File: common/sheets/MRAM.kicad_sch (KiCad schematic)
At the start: 2 parts, among them U11 MR25H10

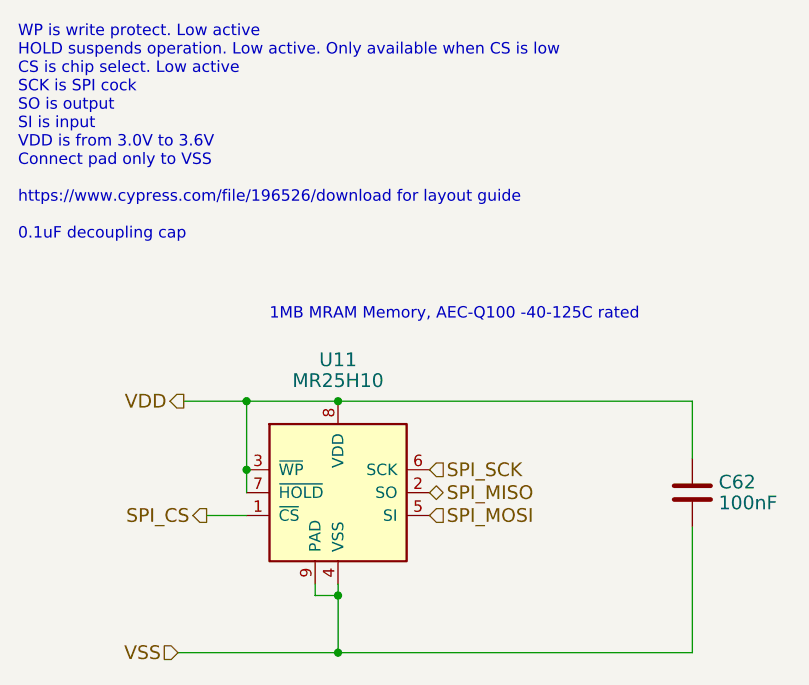
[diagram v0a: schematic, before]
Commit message: move commonly used hierarchical sheets to common/sheets for easy reuse
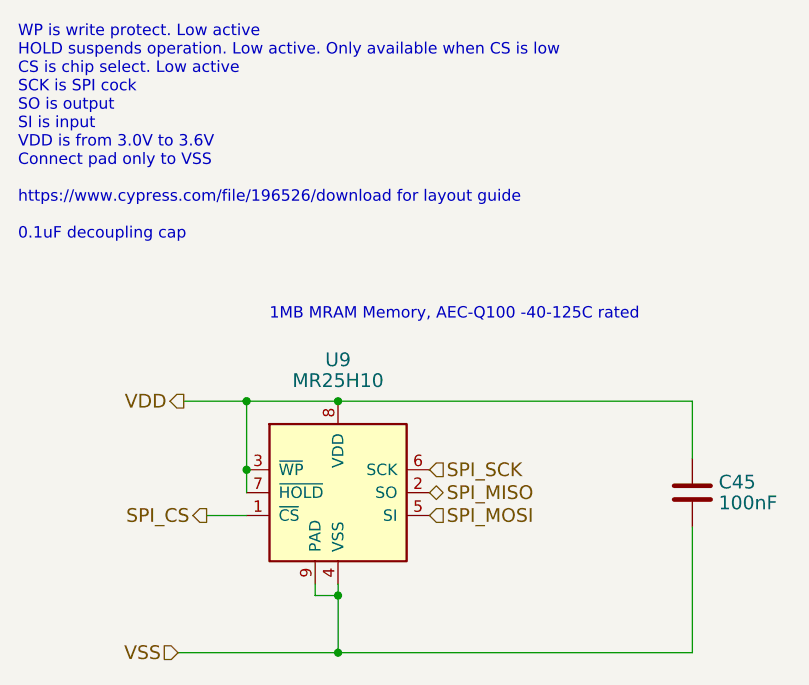
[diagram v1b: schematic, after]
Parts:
- renumbered C62 to C45, U11 to U9
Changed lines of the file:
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@@
 		(on_board yes)
 		(dnp no)
-		(property "Reference" "C62"
+		(property "Reference" "C45"
 			(at 201.041 118.2116 0)
 			(effects
@@
 				)
 			)
-			(project ""
+			(project "comm_board"
 				(path "/a863a5ec-a5d4-4f54-be53-e8c01d5e3ac4/53f12969-e593-459a-9671-cc23a5a9aea0/96ad4f73-2856-49c5-b898-35474412a80c"
 					(reference "C47")
@@
 				)
 			)
-			(project ""
+			(project "AVIONICS_BOARD"
 				(path "/f6cc00ab-17f1-4973-862f-7ac95fe70668/00000000-0000-0000-0000-00005ea31c93/00000000-0000-0000-0000-00006310c53d"
 					(reference "C45")
@@
 		(on_board yes)
 		(dnp no)
-		(property "Reference" "U11"
+		(property "Reference" "U9"
 			(at 158.75 104.6226 0)
 			(effects
@@
 				)
 			)
-			(project ""
+			(project "comm_board"
 				(path "/a863a5ec-a5d4-4f54-be53-e8c01d5e3ac4/53f12969-e593-459a-9671-cc23a5a9aea0/96ad4f73-2856-49c5-b898-35474412a80c"
 					(reference "U9")
@@
 				)
 			)
-			(project ""
+			(project "AVIONICS_BOARD"
 				(path "/f6cc00ab-17f1-4973-862f-7ac95fe70668/00000000-0000-0000-0000-00005ea31c93/00000000-0000-0000-0000-00006310c53d"
 					(reference "U9")

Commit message: absolute paths for includes of includes or the second level common/sheet will cause problems!
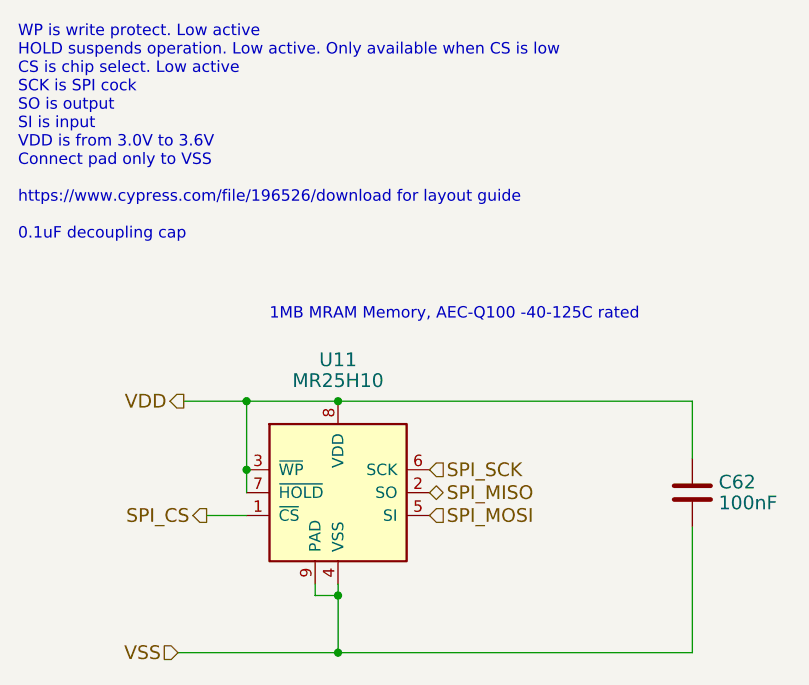
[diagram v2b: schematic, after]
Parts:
- renumbered C45 to C62, U9 to U11
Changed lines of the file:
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@@
 		(on_board yes)
 		(dnp no)
-		(property "Reference" "C45"
+		(property "Reference" "C62"
 			(at 201.041 118.2116 0)
 			(effects
@@
 		)
 		(instances
-			(project ""
+			(project "EPS"
 				(path "/05170af6-30ef-4c3a-b972-f098085da1bc/00000000-0000-0000-0000-00005fbffcb6/00000000-0000-0000-0000-00005ea7cbb1"
 					(reference "C28")
@@
 				)
 			)
-			(project ""
+			(project "sci_board_wo_switches"
 				(path "/b4b2c88d-f6cd-4e60-862d-e21f68728580/f3d5c282-94c3-4259-817b-bad3ee4bc8e5"
 					(reference "C62")
@@
 		(on_board yes)
 		(dnp no)
-		(property "Reference" "U9"
+		(property "Reference" "U11"
 			(at 158.75 104.6226 0)
 			(effects
@@
 		)
 		(instances
-			(project ""
+			(project "EPS"
 				(path "/05170af6-30ef-4c3a-b972-f098085da1bc/00000000-0000-0000-0000-00005fbffcb6/00000000-0000-0000-0000-00005ea7cbb1"
 					(reference "U5")
@@
 				)
 			)
-			(project ""
+			(project "sci_board_wo_switches"
 				(path "/b4b2c88d-f6cd-4e60-862d-e21f68728580/f3d5c282-94c3-4259-817b-bad3ee4bc8e5"
 					(reference "U11")

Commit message: move legacy schema and files into inactive folders for removal
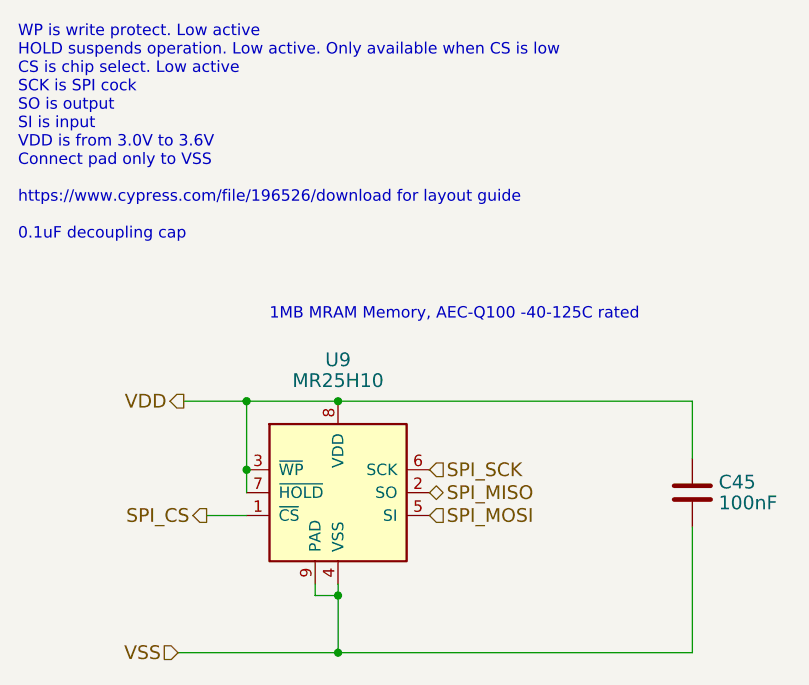
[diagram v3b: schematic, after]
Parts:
- renumbered C62 to C45, U11 to U9
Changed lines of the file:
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@@
 		(on_board yes)
 		(dnp no)
-		(property "Reference" "C62"
+		(property "Reference" "C45"
 			(at 201.041 118.2116 0)
 			(effects
@@
 		(on_board yes)
 		(dnp no)
-		(property "Reference" "U11"
+		(property "Reference" "U9"
 			(at 158.75 104.6226 0)
 			(effects

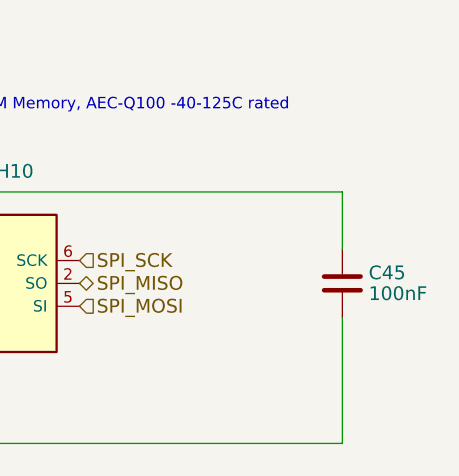
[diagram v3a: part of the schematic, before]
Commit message: moving common sheets to common, cleanup for some missed files
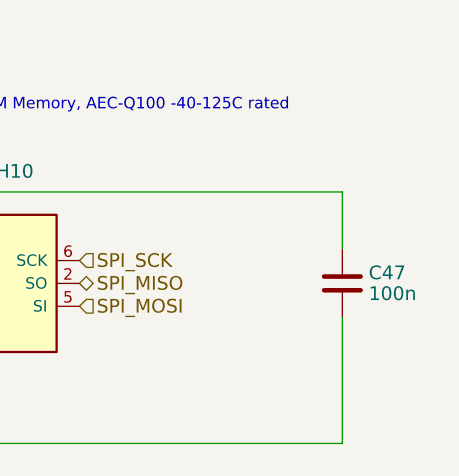
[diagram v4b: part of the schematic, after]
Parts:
- C47: renamed from C45; value 100nF -> 100n
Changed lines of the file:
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@@
 		(on_board yes)
 		(dnp no)
-		(property "Reference" "C45"
+		(property "Reference" "C47"
 			(at 201.041 118.2116 0)
 			(effects
@@
 			)
 		)
-		(property "Value" "100nF"
+		(property "Value" "100n"
 			(at 201.041 120.523 0)
 			(effects

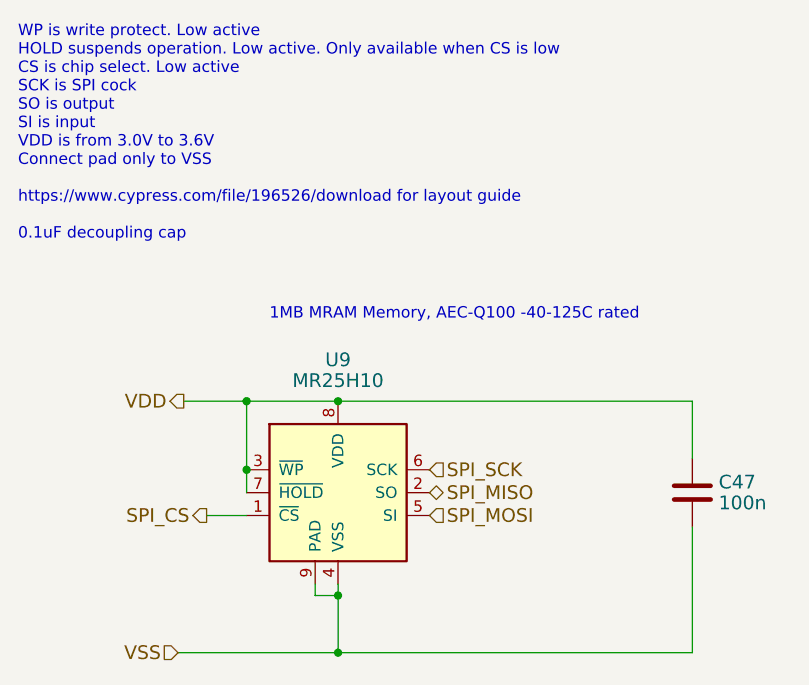
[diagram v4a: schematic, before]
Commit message: cleaning up common sheets and projects. prepare for removal of legacy path links
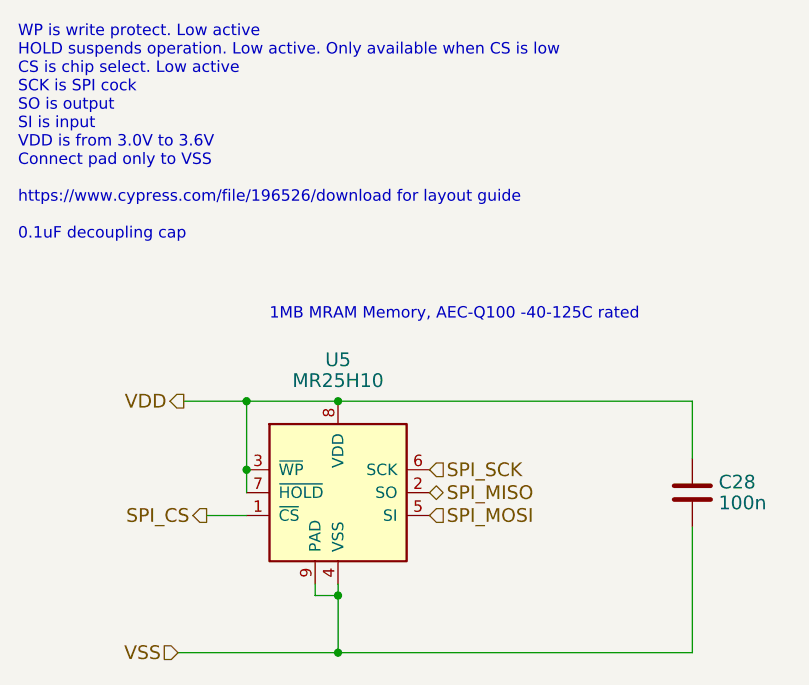
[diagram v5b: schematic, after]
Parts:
- renumbered C47 to C28, U9 to U5
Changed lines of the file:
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@@
 		(on_board yes)
 		(dnp no)
-		(property "Reference" "C47"
+		(property "Reference" "C28"
 			(at 201.041 118.2116 0)
 			(effects
@@
 		(on_board yes)
 		(dnp no)
-		(property "Reference" "U9"
+		(property "Reference" "U5"
 			(at 158.75 104.6226 0)
 			(effects
